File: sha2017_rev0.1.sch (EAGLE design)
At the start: 71 parts, among them IC1 CP210X_USB_UART, IC2 AP7215, IC5 MCP73833, M1 MOTOR10MM, Q1 MMBT2222A, Q2 MMBT2222A, Q4 MOSFET-PCHANNEL, Q5 MMBT2222A, Q6 MOSFET-NCHANNELBSS123LT1G, Q7 MMBT2222A, U1 ESP32MOD, X1_ JST-PH3

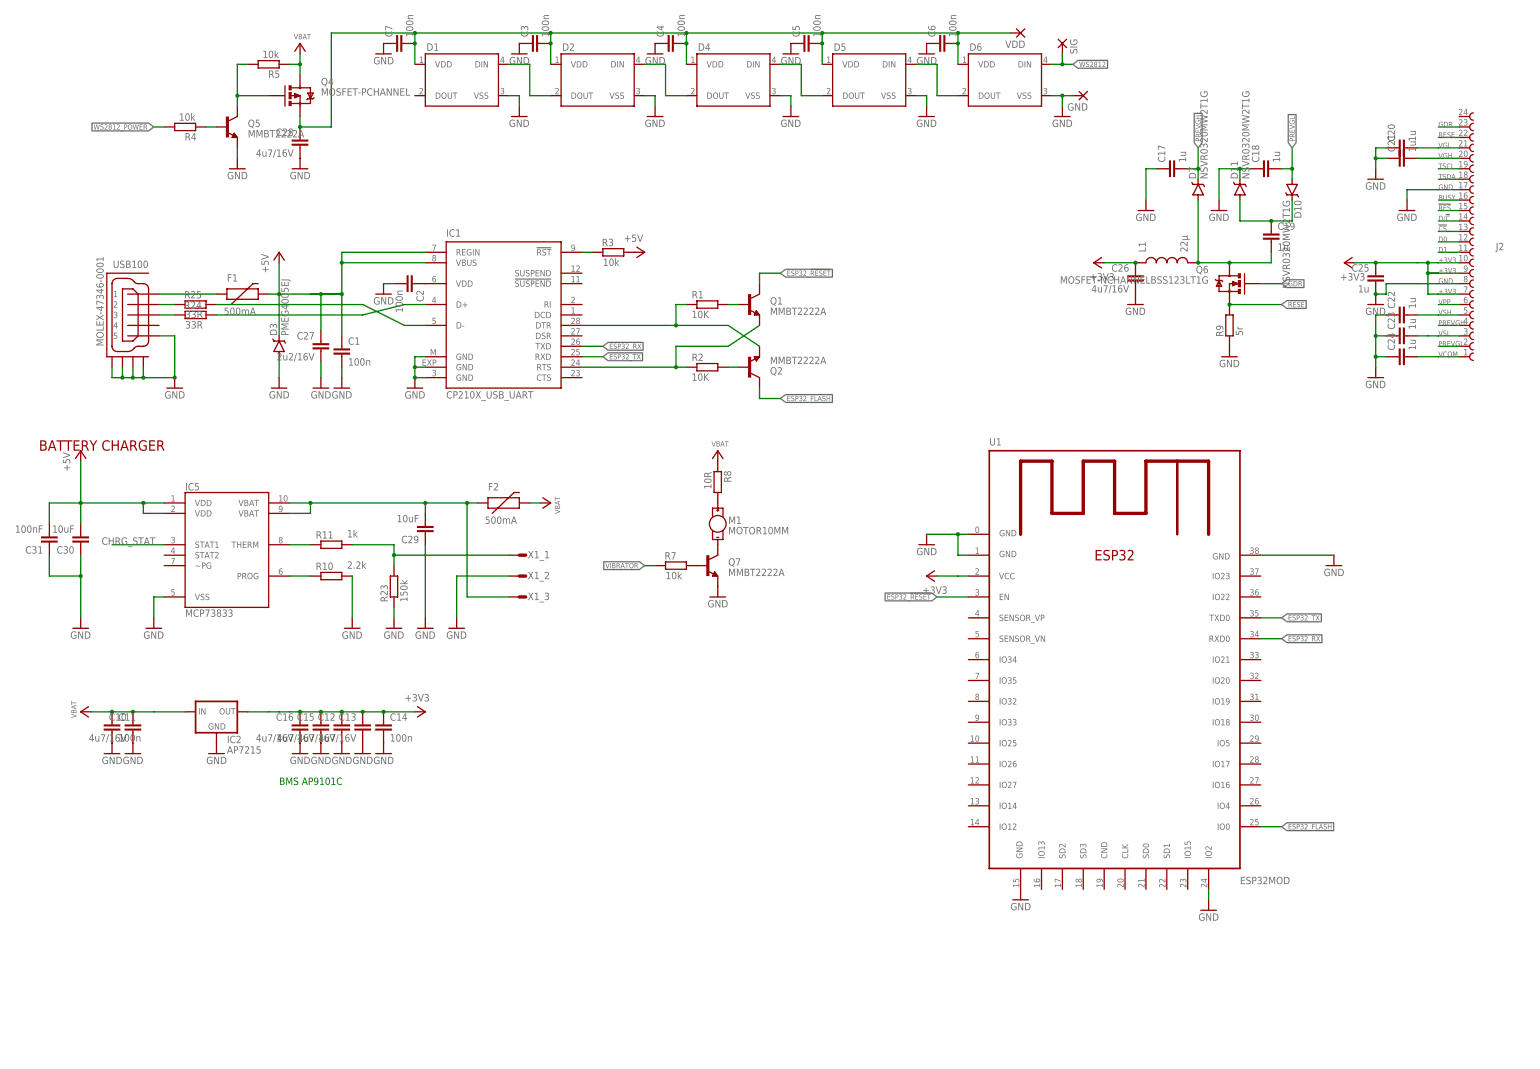
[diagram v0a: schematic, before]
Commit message: add esp32 pinout
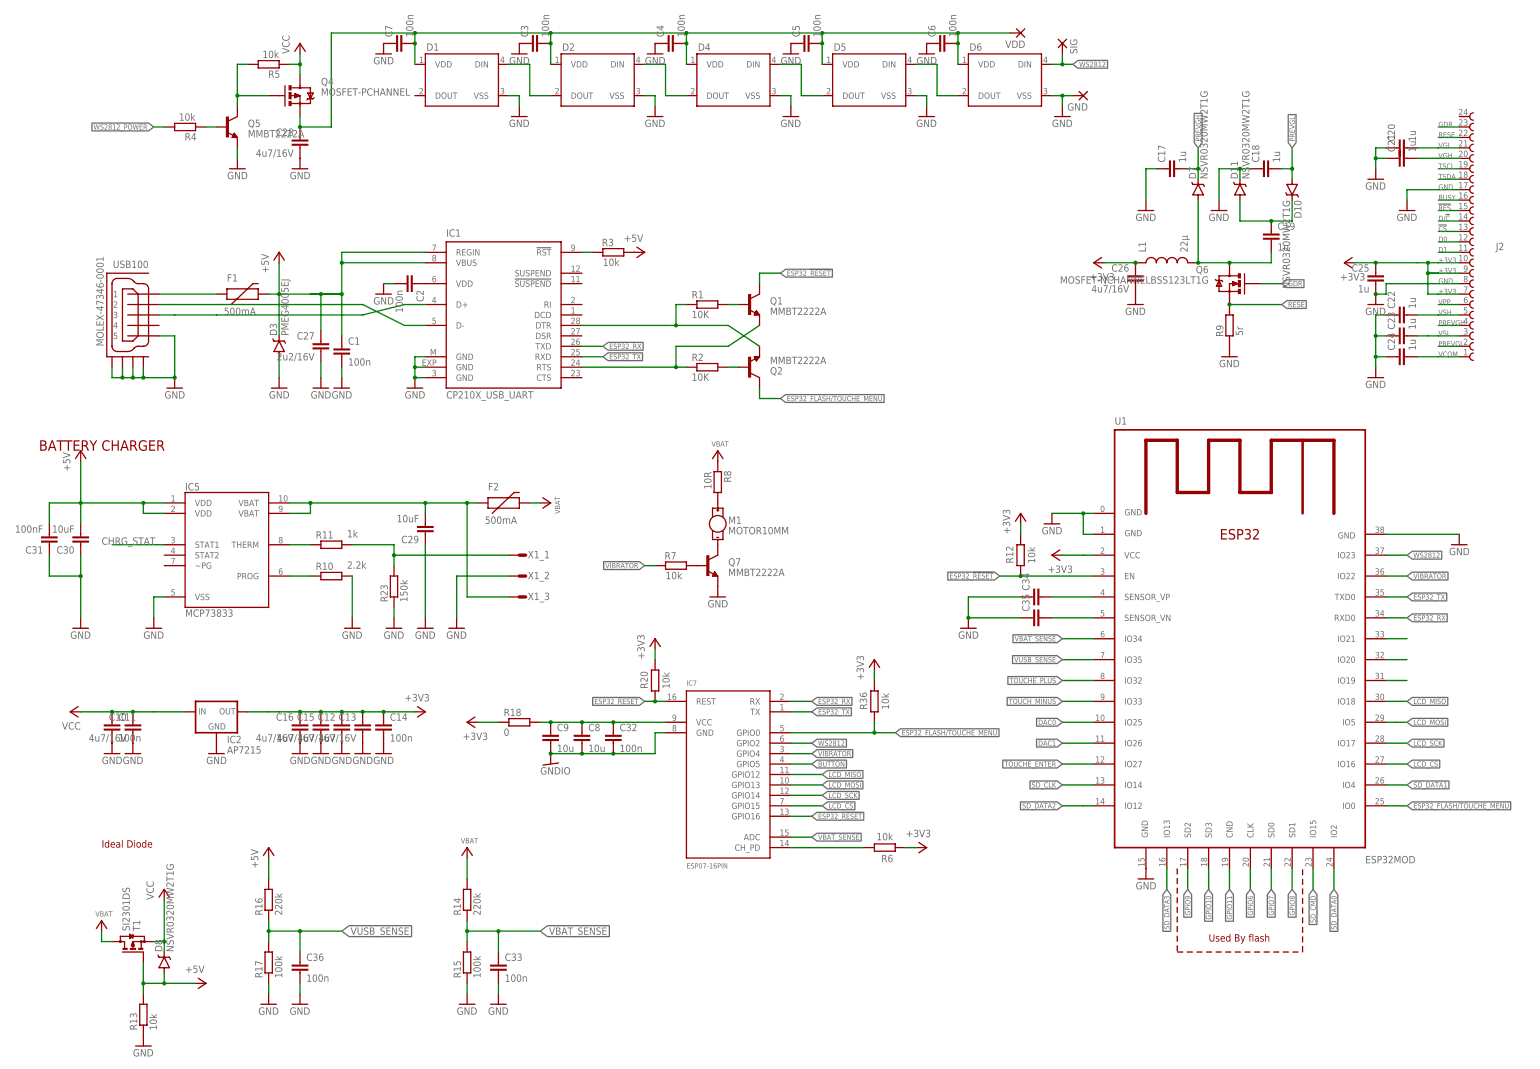
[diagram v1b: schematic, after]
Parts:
- removed R24, R25: 33R, 00ralf:R0603-DASHES
- added C32, C33, C36: 100n, rcl:C-EUC0603
- added C34, C35: (no value), rcl:C-EUC0603
- added C8, C9: 10u, rcl:C-EUC0603
- added D8: NSVR0320MW2T1G, SparkFun-DiscreteSemi:BAT20JFILM
- added IC7: ESP07-16PIN, esp8266modules:ESP07-16PIN
- added R12, R13, R20, R36, R6: 10k, rcl:R-EU_R0603
- added R14, R16: 220k, rcl:R-EU_R0603
- added R15, R17: 100k, rcl:R-EU_R0603
- added R18: 0, rcl:R-EU_R0603
- added T1: SI2301DS, transistor-small-signal:BSS84
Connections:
- removed net ESP32_FLASH: Q2.C, U1.IO0
- removed net USB_DM: IC1.D-, R25.1
- removed net USB_DM_CON: R24.2, USB100.3
- removed net USB_DP: IC1.D+, R24.1
- new net BUTTON: IC7.GPIO5
- new net DAC0: U1.IO25
- new net DAC1: U1.IO26
- new net ESP32_FLASH/TOUCHE_MENU: IC7.GPIO0, Q2.C, R36.2, U1.IO0
- new net GNDIO: C32.2, C8.2, C9.2, IC7.GND
- new net GPIO10: U1.SD3
- new net GPIO11: U1.CND
- new net GPIO19: U1.IO19
- new net GPIO20: U1.IO20
- new net GPIO21: U1.IO21
- new net GPIO6: U1.CLK
- new net GPIO7: U1.SD0
- new net GPIO8: U1.SD1
- new net GPIO9: U1.SD2
- new net LCD_CS: IC7.GPIO15, U1.IO16
- new net LCD_MISO: IC7.GPIO12, U1.IO18
- new net LCD_MOSI: IC7.GPIO13, U1.IO5
- new net LCD_SCK: IC7.GPIO14, U1.IO17
- new net N$26: C34.2, U1.SENSOR_VP
- new net N$27: C35.2, U1.SENSOR_VN
- new net N$46: C32.1, C8.1, C9.1, IC7.VCC, R18.2
- new net N$7: IC7.CH_PD, R6.1
- new net SD_CLK: U1.IO14
- new net SD_CMD: U1.IO15
- new net SD_DATA0: U1.IO2
- new net SD_DATA1: U1.IO4
- new net SD_DATA2: U1.IO12
- new net SD_DATA3: U1.IO13
- new net TOUCHE_ENTER: U1.IO27
- new net TOUCHE_PLUS: U1.IO32
- new net TOUCH_MINUS: U1.IO33
- new net USB_DN_CON: IC1.D-, USB100.2
- new net VBAT_SENSE: C33.1, IC7.ADC, R14.1, R15.2, U1.IO34
- new net VCC: C10.1, C11.1, D8.C, IC2.IN, Q4.D, R5.2, T1.S
- new net VUSB_SENSE: C36.1, R16.1, R17.2, U1.IO35
- net +3V3: now also R12.1, R18.1, R20.1, R36.1, R6.2
- net +5V: now also D8.A, R13.2, R16.2, T1.G
- net ESP32_!RESET: now also IC7.GPIO16, IC7.REST, R12.2, R20.2
- net ESP32_RX: now also IC7.RX
- net ESP32_TX: now also IC7.TX
- net GND: now also C33.2, C34.1, C35.1, C36.2, R13.1, R15.1, R17.1; no longer U1.IO2
- net USB_DP_CON: now also IC1.D+, USB100.3; no longer R25.2, USB100.2
- net VBAT: now also R14.2, T1.D; no longer C10.1, C11.1, IC2.IN, Q4.D, R5.2
- net VIBRATOR: now also IC7.GPIO4, U1.IO22
- net WS2812: now also IC7.GPIO2, U1.IO23
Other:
- note added: "Ideal Diode"
- note added: "Used By flash"
- note removed: "BMS AP9101C"
- moved on the sheet: U1

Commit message: schematic Cleanup adding MPU6050
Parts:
- added C37, C39: 0.1uF, SparkFun:CAP0603-CAP
- added C38: 2.2nF, SparkFun:CAP0603-CAP
- added C40: 10nF, SparkFun:CAP0603-CAP
- added R19, R21: 4k7, 00ralf:R0603-DASHES
- added R714: 100k, rcl:R-EU_R0402
- added SJ1: (no value), SparkFun:SOLDERJUMPER_2WAYPASTE2&3
- added U2: MPU-6050-1, Testing:MPU-6050-1
- added X701: 2908-05WB-MG, con-3m:2908-05WB-MG
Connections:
- removed net DAC0: U1.IO25
- removed net DAC1: U1.IO26
- removed net GPIO19: U1.IO19
- removed net GPIO20: U1.IO20
- removed net GPIO21: U1.IO21
- new net ADO: SJ1.2, U2.AD0
- new net AUX_SCL: U2.AUX_CL
- new net AUX_SDA: U2.AUX_DA
- new net I2C_SCL: R19.1, U1.IO21, U2.SCL
- new net I2C_SDA: R21.1, U1.IO20, U2.SDA
- new net MPU_INT: U1.IO25, U2.INT
- new net N$24: C38.1, U2.CPOUT
- new net N$25: C37.1, U2.REGOUT
- new net N$28: U2.VDD
- new net SD_CD: R714.2, U1.IO16, X701.SHIELD@1
- new net SD_DAT0: X701.DO
- new net SD_DAT1: X701.RSV
- new net SD_DAT2: X701.NC
- new net SD_DAT3: X701.CS
- new net VIO: C40.1, U2.VLOGIC
- net +3V3: now also C39.1, R19.2, R21.2, SJ1.1
- net GND: now also C37.2, C38.2, C39.2, C40.2, SJ1.3, U2.CLKIN, U2.FSYNC, U2.GND, X701.GND, X701.SHIELD@2, X701.SHIELD@3, X701.SHIELD@4
- net LCD_CS: now also U1.IO17; no longer U1.IO16
- net LCD_MISO: now also U1.IO19; no longer U1.IO18
- net LCD_MOSI: now also U1.IO18; no longer U1.IO5
- net LCD_SCK: now also U1.IO5; no longer U1.IO17
- net SD_CLK: now also X701.SCK
- net SD_CMD: now also X701.DI
- net VCC: now also R714.1, X701.VCC
- net VIBRATOR: now also U1.IO26; no longer U1.IO22
- net WS2812_POWER: now also U1.IO22
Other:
- note added: "*"
- note added: "E-Paper Display"
- note added: "I2C Address Selection*"
- note added: "IMU"
- note added: "MCU/WIFI"
- note added: "MISC"
- note added: "POWER SUPPLY"
- note added: "RTC Crystal"
- note added: "SD card"
- note added: "USB Seriell"
- note added: "Vibrator"
- note added: "Voltag Regulator"
- note added: "Voltage sensing"
- note added: "WS2812"
